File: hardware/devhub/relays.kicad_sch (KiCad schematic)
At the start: 13 parts, among them J5 Banana COM 1, J6 Banana NC 1, J7 Banana COM 2, J8 Banana NC 2, K1 G5Q-1 DC5, K2 G5Q-1 DC5, U9 ULN2003A

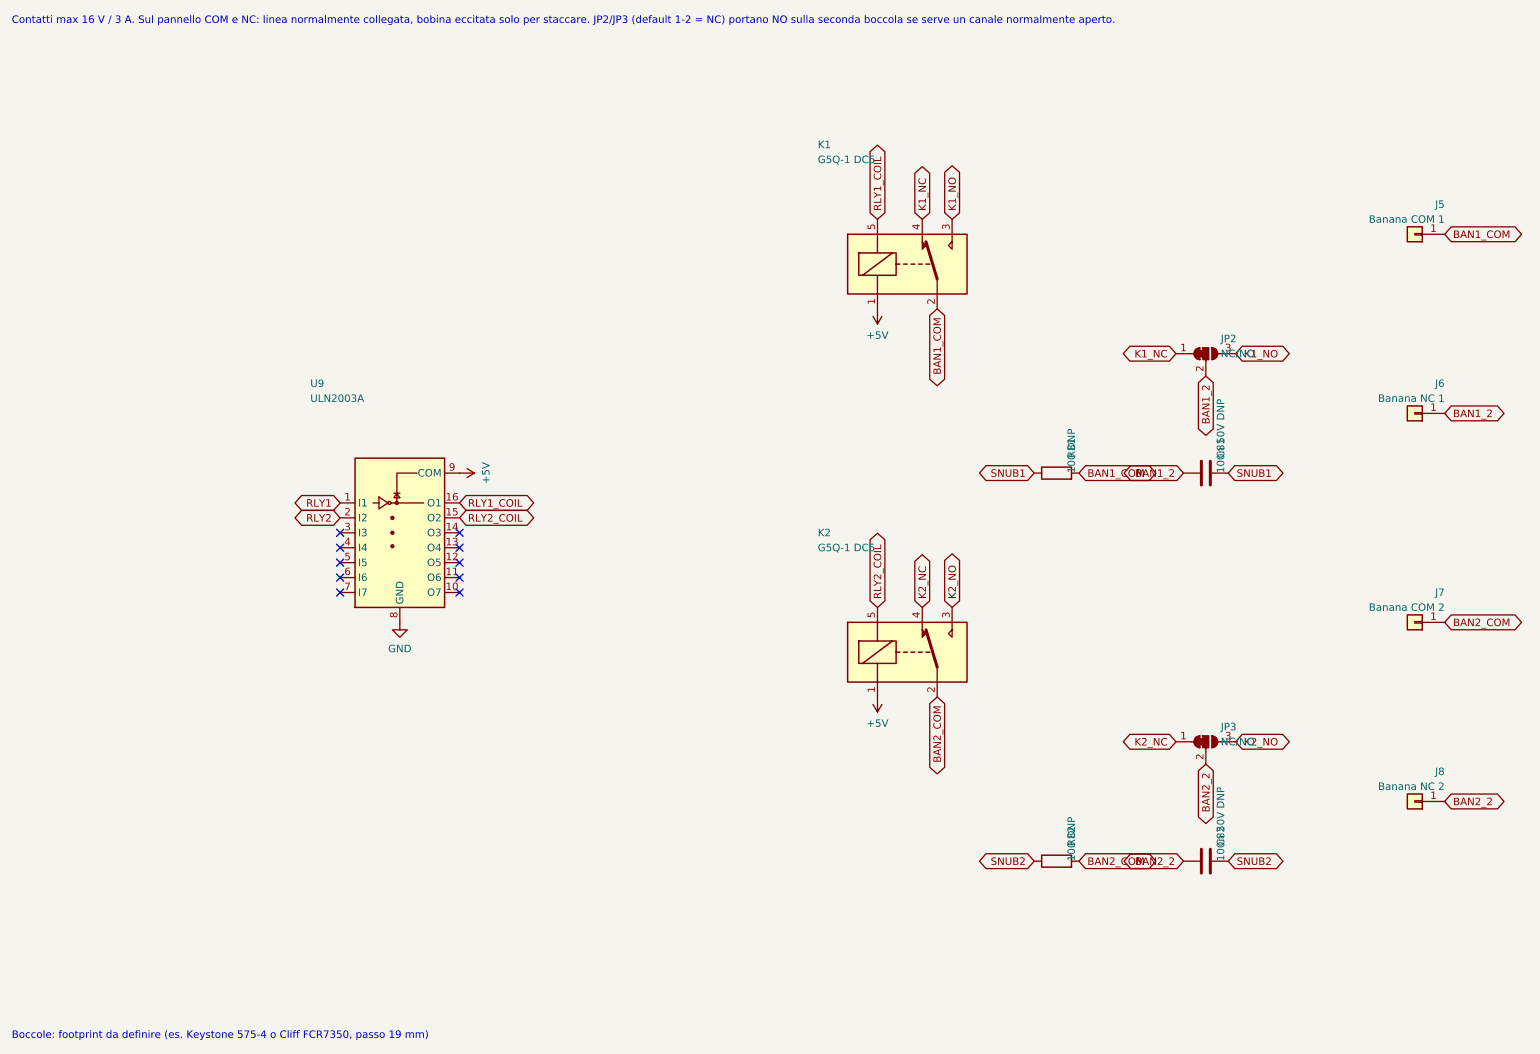
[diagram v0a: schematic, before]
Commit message: Schematic v0.2: hub reset supervisor, 1 A LDO, reorganized sheets, USB connectors and crystal
Functional changes:
- USB2517 RESET_N with pull-up and MCP120T-300 supervisor, wired-OR with
  the MCU (open-drain): resetting the MCU no longer resets the hub, so the
  ST DFU bootloader is reachable through it (D16/D17).
- 3.3 V LDO: AP7361C-33E (1 A, SOT-223) instead of AP2112K, which
  dissipated too much with the hub load.
- 74HC595 /OE on PB6 with pull-up: LEDs off until firmware enables them.
- Orange D93 instead of blue, USB-A bulk capacitance >= 120 uF, relay coil
  pinout fixed, snubbers marked DNP, Cliff FCR7350 banana jack footprints.
- D18: horizontal USB connectors, GCT USB4105-GF-A (USB-C) and Kycon
  KUSBX-AS1N-B (USB-A).
- D19: YXC X322524MOB4SI 24 MHz crystal (C_L 12 pF), 15 pF C0G load caps.

Layout: nearby parts wired directly, every net still explicitly named;
local labels inside sheets, global only across sheets, hierarchical for
ports. Files saved with KiCad 10.

Connectivity checked against the previous netlist, ERC clean.
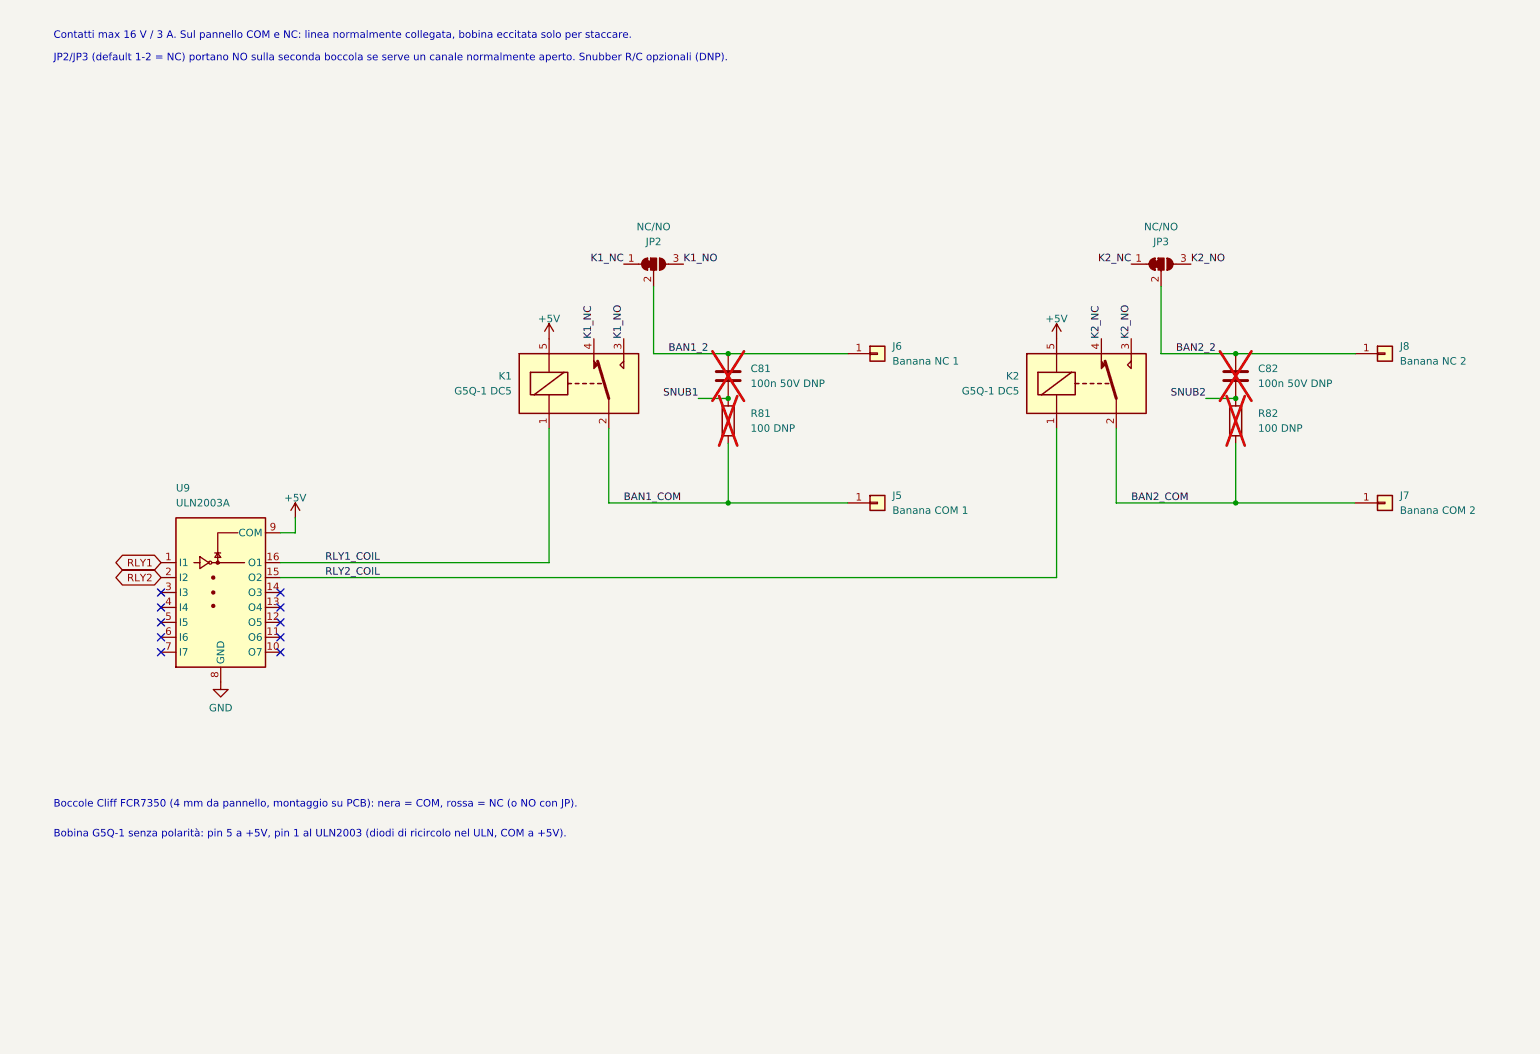
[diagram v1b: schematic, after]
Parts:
- C81, C82, R81, R82: now not fitted
- J5, J7: footprint (none) -> Connector:Banana_Cliff_FCR7350B_S16N-PC_Horizontal
- J6, J8: footprint (none) -> Connector:Banana_Cliff_FCR7350R_S16N-PC_Horizontal
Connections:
- net +5V: now also K1.5, K2.5; no longer K1.1, K2.1
- net RLY1_COIL: now also K1.1; no longer K1.5
- net RLY2_COIL: now also K2.1; no longer K2.5
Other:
- note added: "Bobina G5Q-1 senza polarità: pin 5 a +5V, pin 1 al ULN2003 (diodi di ricircolo nel ULN, COM a +5V)."
- note added: "Boccole Cliff FCR7350 (4 mm da pannello, montaggio su PCB): nera = COM, rossa = NC (o NO con JP)."
- note added: "Contatti max 16 V / 3 A. Sul pannello COM e NC: linea normalmente collegata, bobina eccitata solo per staccare."
- note added: "JP2/JP3 (default 1-2 = NC) portano NO sulla seconda boccola se serve un canale normalmente aperto. Snubber R/C opzionali (DNP)."
- note removed: "Boccole: footprint da definire (es. Keystone 575-4 o Cliff FCR7350, passo 19 mm)"
- note removed: "Contatti max 16 V / 3 A. Sul pannello COM e NC: linea normalmente collegata, bobina eccitata solo per staccare. JP2/JP3 (default 1-2 = NC) portano NO sulla seconda boccola se serve un canale normalmente aperto."

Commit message: Lab-use protection: TPS259470A input eFuse, PI3USB4002A data switches; AGENTS.md
Power input (D20, D21):
- TPS259470A eFuse after the shunt: trips above 5.84 V and below 4.0 V,
  zener on EN to withstand up to 28 V, 3.5 A limit, ~5 ms soft start,
  auto-retry, FLT to the MCU on PB1.
- The shunt stays before the eFuse, so the INA3221 still measures the input
  voltage when the eFuse is off.

Ports (D22): PI3USB4002A instead of TS3USB30E. The connector side withstands
24 V and opens above 4.75 V, so a D+/D- short to VBUS on a board under test
no longer reaches the 3.3 V rail.

Symbols for both ICs added to the project library. AGENTS.md added: the
schematic is edited in KiCad or with targeted changes, never regenerated by
script. Sheets re-saved by KiCad.

Connectivity checked against the previous netlist, ERC clean.
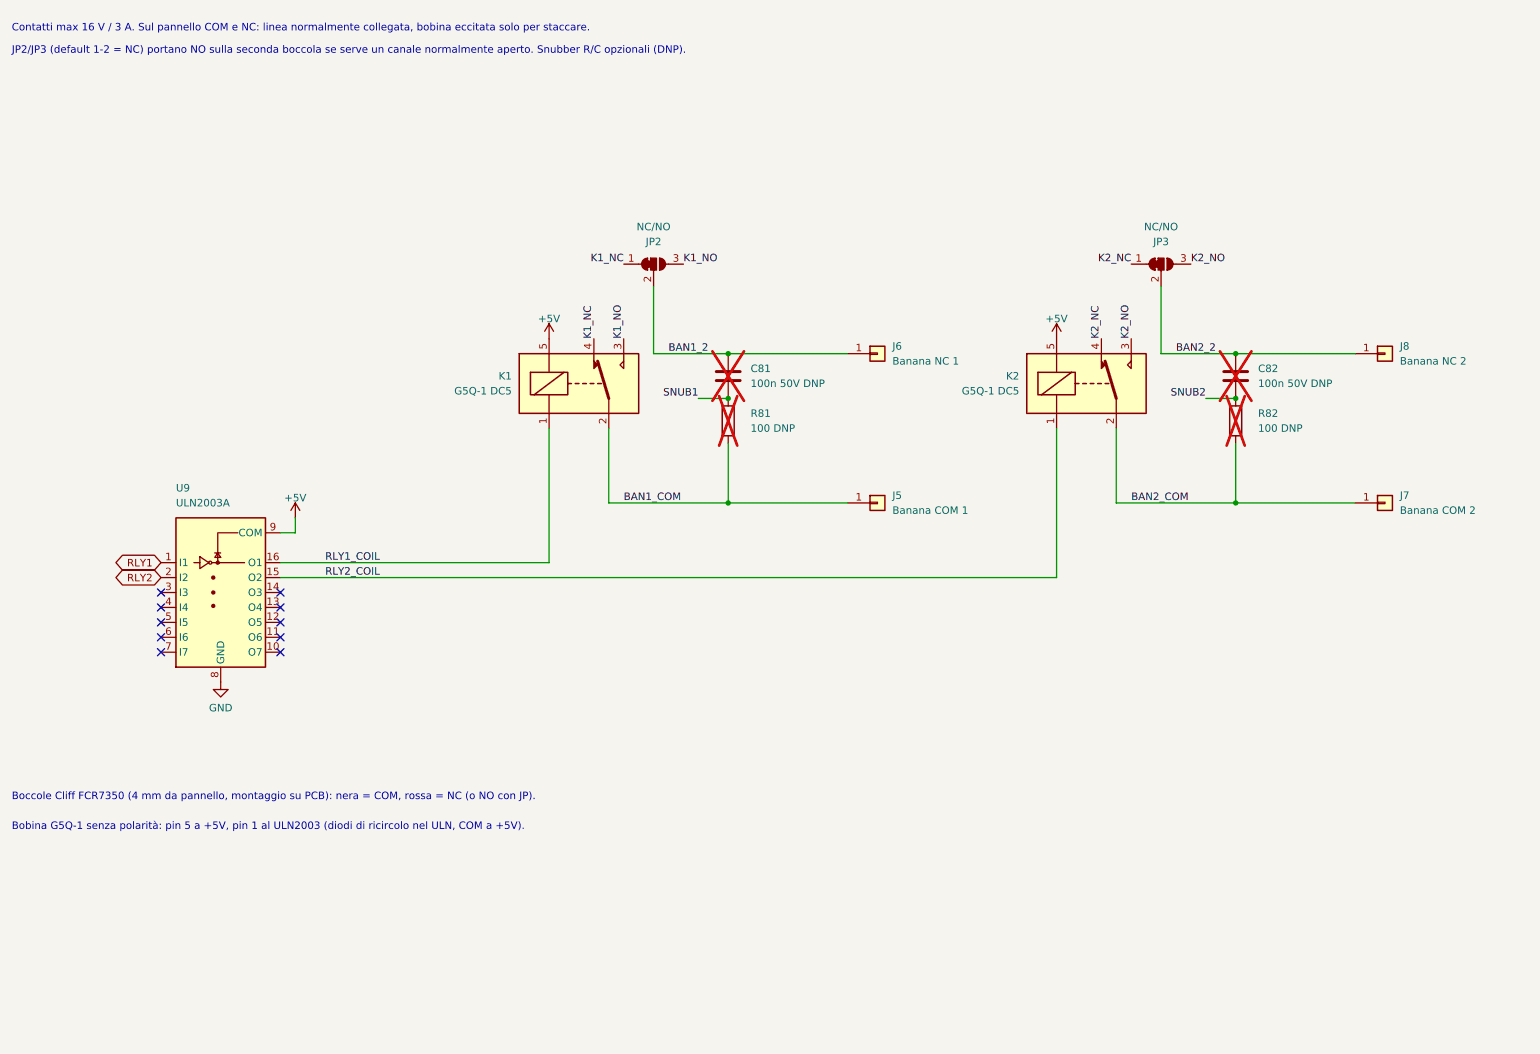
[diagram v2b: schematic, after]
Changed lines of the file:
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@@
 	(text "Bobina G5Q-1 senza polarità: pin 5 a +5V, pin 1 al ULN2003 (diodi di ricircolo nel ULN, COM a +5V)."
 		(exclude_from_sim no)
-		(at 17.272 153.67 0)
+		(at 10.16 152.4 0)
 		(effects
 			(font
@@
 	(text "JP2/JP3 (default 1-2 = NC) portano NO sulla seconda boccola se serve un canale normalmente aperto. Snubber R/C opzionali (DNP)."
 		(exclude_from_sim no)
-		(at 17.272 21.59 0)
+		(at 10.16 20.32 0)
 		(effects
 			(font
@@
 	(text "Boccole Cliff FCR7350 (4 mm da pannello, montaggio su PCB): nera = COM, rossa = NC (o NO con JP)."
 		(exclude_from_sim no)
-		(at 17.272 148.59 0)
+		(at 10.16 147.32 0)
 		(effects
 			(font
@@
 	(text "Contatti max 16 V / 3 A. Sul pannello COM e NC: linea normalmente collegata, bobina eccitata solo per staccare."
 		(exclude_from_sim no)
-		(at 17.272 17.78 0)
+		(at 10.16 16.51 0)
 		(effects
 			(font
@@
 		(in_pos_files yes)
 		(dnp no)
-		(property "Reference" "#PWR130"
+		(property "Reference" "#PWR137"
 			(at 101.6 68.58 0)
 			(hide yes)
@@
 			(project "devhub"
 				(path "/af6ea7d8-d1ba-5fc6-aec8-abf514847630/754ef4c0-187b-5738-814a-57c901f66789"
-					(reference "#PWR130")
+					(reference "#PWR137")
 					(unit 1)
 				)
@@
 		(in_pos_files yes)
 		(dnp no)
-		(property "Reference" "#PWR131"
+		(property "Reference" "#PWR138"
 			(at 187.96 68.58 0)
 			(hide yes)
@@
 			(project "devhub"
 				(path "/af6ea7d8-d1ba-5fc6-aec8-abf514847630/754ef4c0-187b-5738-814a-57c901f66789"
-					(reference "#PWR131")
+					(reference "#PWR138")
 					(unit 1)
 				)
@@
 		(in_pos_files yes)
 		(dnp no)
-		(property "Reference" "#PWR128"
+		(property "Reference" "#PWR135"
 			(at 45.72 127 0)
 			(hide yes)
@@
 			(project "devhub"
 				(path "/af6ea7d8-d1ba-5fc6-aec8-abf514847630/754ef4c0-187b-5738-814a-57c901f66789"
-					(reference "#PWR128")
+					(reference "#PWR135")
 					(unit 1)
 				)
@@
 		(in_pos_files yes)
 		(dnp no)
-		(property "Reference" "#PWR129"
+		(property "Reference" "#PWR136"
 			(at 58.42 99.06 0)
 			(hide yes)
@@
 			(project "devhub"
 				(path "/af6ea7d8-d1ba-5fc6-aec8-abf514847630/754ef4c0-187b-5738-814a-57c901f66789"
-					(reference "#PWR129")
+					(reference "#PWR136")
 					(unit 1)
 				)

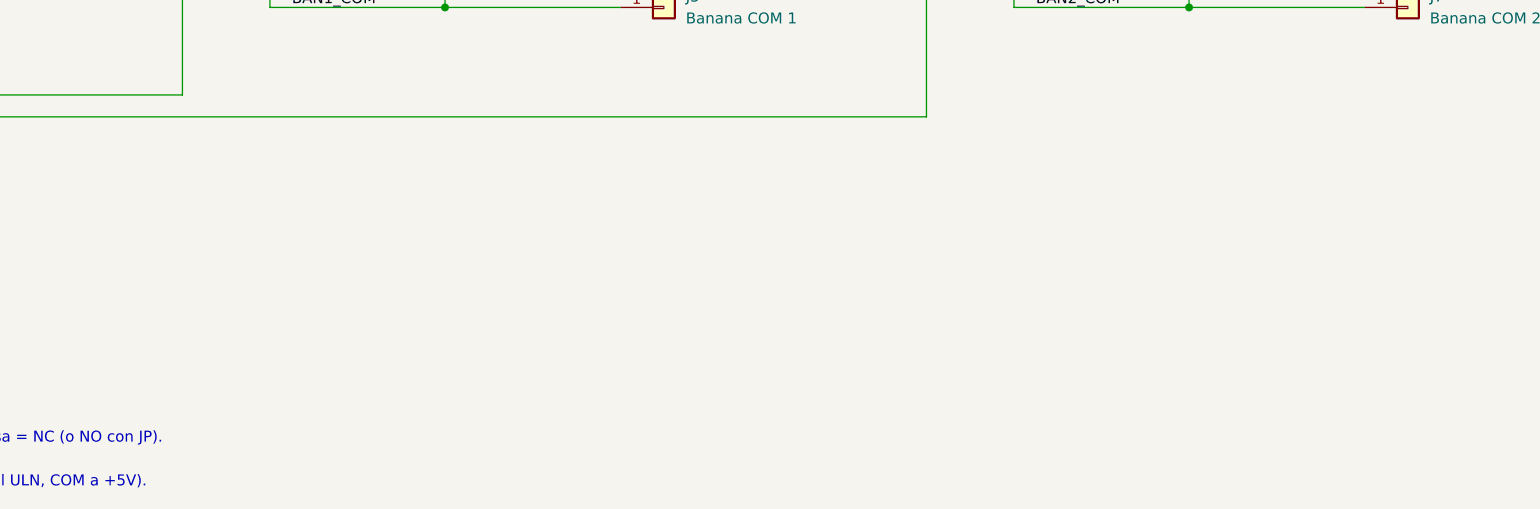
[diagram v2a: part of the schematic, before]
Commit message: SMAJ20A input TVS, no TVS on ports (D24, D25); relay push buttons (D26)
- The SMAJ5.0A already conducted at ~6.4 V and would burn with a 12-20 V
  supply before the eFuse trips; the SMAJ20A lets the eFuse do its job.
  No TVS on ports: it does not help against a sustained back-fed voltage.
  Two LEDs per port confirmed.
- SW1/SW2 on PB12/PB13 toggle the relays; new requirement RF-17 on panel
  buttons, RELAY_CHANGED event in the protocol.

Targeted schematic changes, connectivity otherwise unchanged, ERC clean.
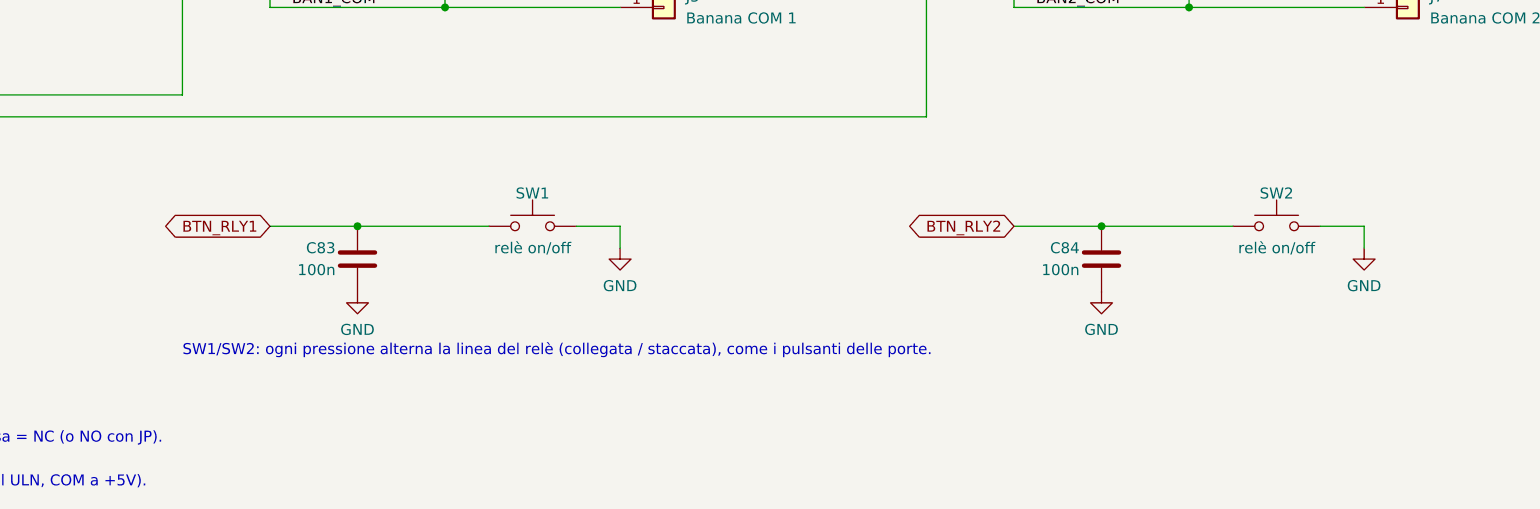
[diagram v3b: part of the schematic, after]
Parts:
- added C83, C84: 100n, Capacitor_SMD:C_0603_1608Metric, symbol Device:C
- added SW1, SW2: relè on/off, Button_Switch_THT:SW_PUSH_6mm_H13mm, symbol Switch:SW_Push
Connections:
- net GND: now also C83.2, C84.2, SW1.2, SW2.2
- new net BTN_RLY1: C83.1, SW1.1
- new net BTN_RLY2: C84.1, SW2.1
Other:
- note added: "SW1/SW2: ogni pressione alterna la linea del relè (collegata / staccata), come i pulsanti delle porte."
